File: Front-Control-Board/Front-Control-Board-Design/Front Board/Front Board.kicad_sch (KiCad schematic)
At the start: 16 parts, among them J1 Conn_01x08, J2 Conn_01x23, U1 MAX33054EASA+T, U2 NCP1117-5.0_TO252, U3 ESP32-WROOM-32D

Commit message: front board update
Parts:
- added D? (x3): 1N630xCA, Diode_THT:D_DO-201AE_P15.24mm_Horizontal, symbol Diode:1N630xCA
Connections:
- net Brake_1: now also D?.2 (K)
- net CAN_RX: now also U3.17 (SHD/SD2)
- net CAN_TX: now also U3.18 (SWP/SD3)
- net D+: now also D?.1 (A1)
- net D-: now also D?.1 (A1)
- net GND: now also D?.1 (A1), D?.2 (A2), D?.2 (A2)
- net L_wheel: now also D?.1 (K)
- net R_sus: now also D?.2 (K)
- net R_wheel: now also D?.1 (K)
- net VBUS: now also D?.2 (A2)
- net LORA_RX: now reaches U3.27 (IO16)
- net LORA_TX: now reaches U3.28 (IO17)
- net LORA NSS: now reaches U3.30 (IO18)
- net LORA Reset: now reaches U3.31 (IO19)
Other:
- removed sheet USB interface
- added sheet USB-interface (USB-interface.kicad_sch)
- moved on the sheet: D?

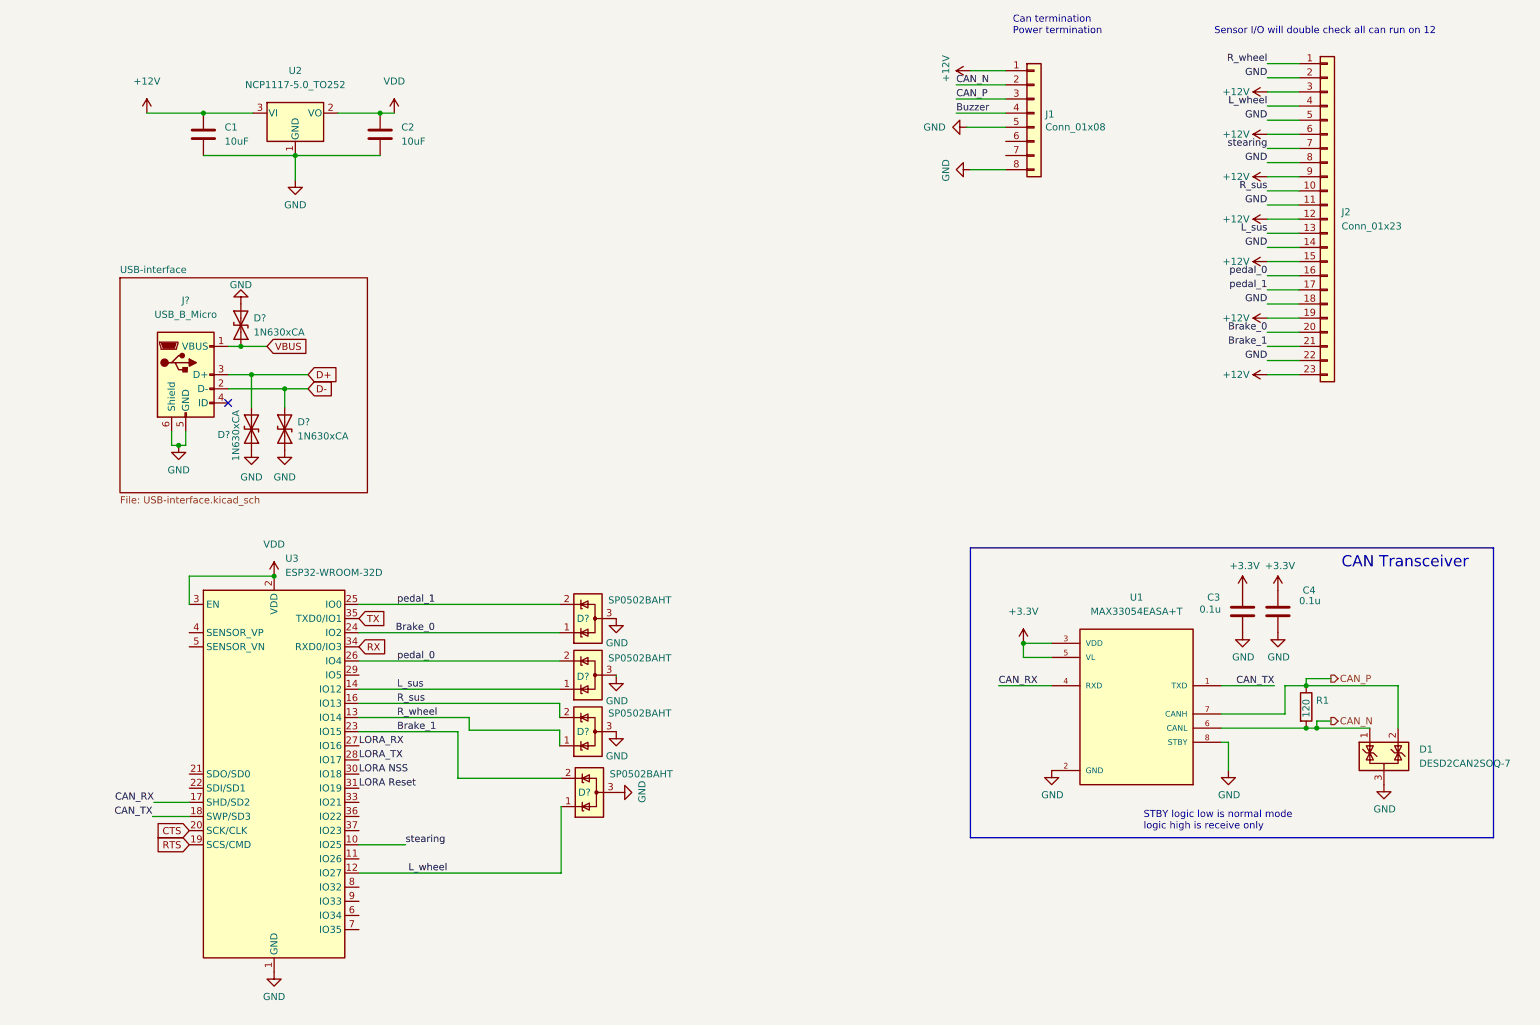
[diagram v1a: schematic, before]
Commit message: Front board finished schematic
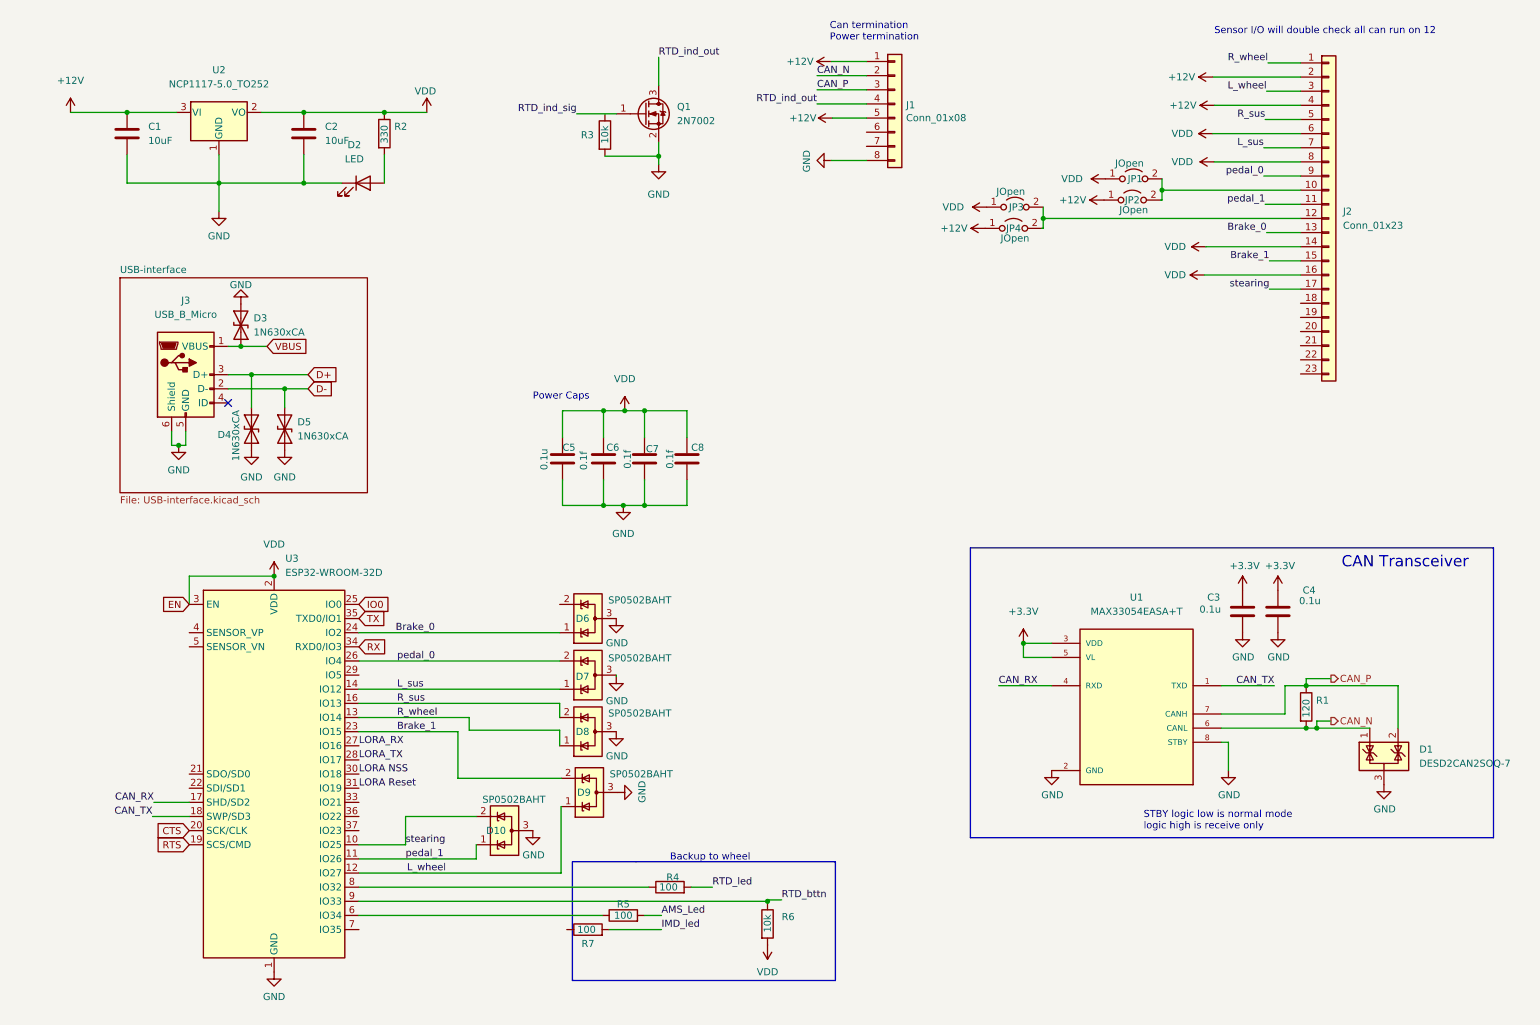
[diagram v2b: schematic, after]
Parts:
- added C5: 0.1u, Capacitor_SMD:C_0603_1608Metric_Pad1.08x0.95mm_HandSolder, symbol Device:C
- added C6, C7, C8: 0.1f, Capacitor_SMD:C_0603_1608Metric_Pad1.08x0.95mm_HandSolder, symbol Device:C
- added D10: SP0502BAHT, Package_TO_SOT_SMD:SOT-23, symbol Power_Protection:SP0502BAHT
- added D2: LED, LED_SMD:LED_0603_1608Metric_Pad1.05x0.95mm_HandSolder, symbol Device:LED
- added JP1, JP2, JP3, JP4: JOpen, TestPoint:TestPoint_2Pads_Pitch2.54mm_Drill0.8mm, symbol Jumper:Jumper_2_Open
- added Q1: 2N7002, Package_TO_SOT_SMD:SOT-23, symbol Transistor_FET:2N7002
- added R2: 330, Resistor_SMD:R_0603_1608Metric_Pad0.98x0.95mm_HandSolder, symbol Device:R
- added R3, R6: 10k, Resistor_SMD:R_0603_1608Metric_Pad0.98x0.95mm_HandSolder, symbol Device:R
- added R4, R5, R7: 100, Resistor_SMD:R_0603_1608Metric_Pad0.98x0.95mm_HandSolder, symbol Device:R
- J3: renamed from J?; footprint (none) -> Connector_USB:USB_Micro-B_Wuerth_614105150721_Vertical
- gave numbers to parts that had none: 7
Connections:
- net +12V: now also J1.5 (Pin_5), J2.2 (Pin_2), J2.4 (Pin_4), JP2.1 (A), JP4.1 (A); no longer J2.12 (Pin_12), J2.15 (Pin_15), J2.19 (Pin_19), J2.23 (Pin_23), J2.3 (Pin_3), J2.6 (Pin_6), J2.9 (Pin_9)
- net Brake_0: now also J2.13 (Pin_13); no longer J2.20 (Pin_20)
- net Brake_1: now also J2.15 (Pin_15); no longer J2.21 (Pin_21)
- net GND: now also C5.2, C6.2, C7.2, C8.2, D10.3 (A), D2.1 (K), Q1.2 (S), R3.2; no longer J1.5 (Pin_5), J2.11 (Pin_11), J2.14 (Pin_14), J2.18 (Pin_18), J2.2 (Pin_2), J2.22 (Pin_22), J2.5 (Pin_5), J2.8 (Pin_8)
- net L_sus: now also J2.7 (Pin_7); no longer J2.13 (Pin_13)
- net L_wheel: now also J2.3 (Pin_3); no longer J2.4 (Pin_4)
- net R_sus: now also J2.5 (Pin_5); no longer J2.10 (Pin_10)
- net VDD: now also J2.14 (Pin_14), J2.16 (Pin_16), J2.6 (Pin_6), J2.8 (Pin_8), C5.1, C6.1, C7.1, C8.1, JP1.1 (A), JP3.1 (A), R2.1, R6.2
- net pedal_0: now also J2.9 (Pin_9); no longer J2.16 (Pin_16)
- net pedal_1: now also J2.11 (Pin_11), U3.11 (IO26), D10.1 (K); no longer D6.2 (K), J2.17 (Pin_17), U3.25 (IO0)
- net stearing: now also J2.17 (Pin_17), D10.2 (K); no longer J2.7 (Pin_7)
- net at U3.6 (IO34): now also R5.1
- net at U3.8 (IO32): now also R4.1
- net RTD_bttn: now reaches U3.9 (IO33)
- net RTD_bttn: now also R6.1
- net Buzzer renamed RTD_ind_out
- net RTD_ind_out: now also Q1.3 (D)
- new net: J2.10 (Pin_10), JP1.2 (B), JP2.2 (B)
- new net: J2.12 (Pin_12), JP3.2 (B), JP4.2 (B)
- new net: D2.2 (A), R2.2
- new net AMS_Led: R5.2
- new net IMD_led: R7.2
- new net IO0: U3.25 (IO0)
- new net RTD_ind_sig: Q1.1 (G)
- new net RTD_led: R4.2
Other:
- note added: "Backup to wheel"
- note added: "Power Caps"
- moved on the sheet: C1, C2, J1, U2

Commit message: Front board schematic
and linking to footprint done
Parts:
- J2: footprint (none) -> AERO_Footprints:TE_1-770669-1_23pin_Horizontal
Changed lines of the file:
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@@
       (effects (font (size 1.27 1.27)) (justify left))
     )
-    (property "Footprint" "" (id 2) (at 249.174 52.578 0)
+    (property "Footprint" "AERO_Footprints:TE_1-770669-1_23pin_Horizontal" (id 2) (at 249.174 52.578 0)
       (effects (font (size 1.27 1.27)) hide)
     )
@@
     )
     (path "/197899a5-be91-4fa9-8e75-522cf68d1072"
-      (reference "J2") (unit 1) (value "Conn_01x23") (footprint "")
+      (reference "J2") (unit 1) (value "Conn_01x23") (footprint "AERO_Footprints:TE_1-770669-1_23pin_Horizontal")
     )
     (path "/5026d5ac-936b-4ec5-ab91-2c1c820a0f48"

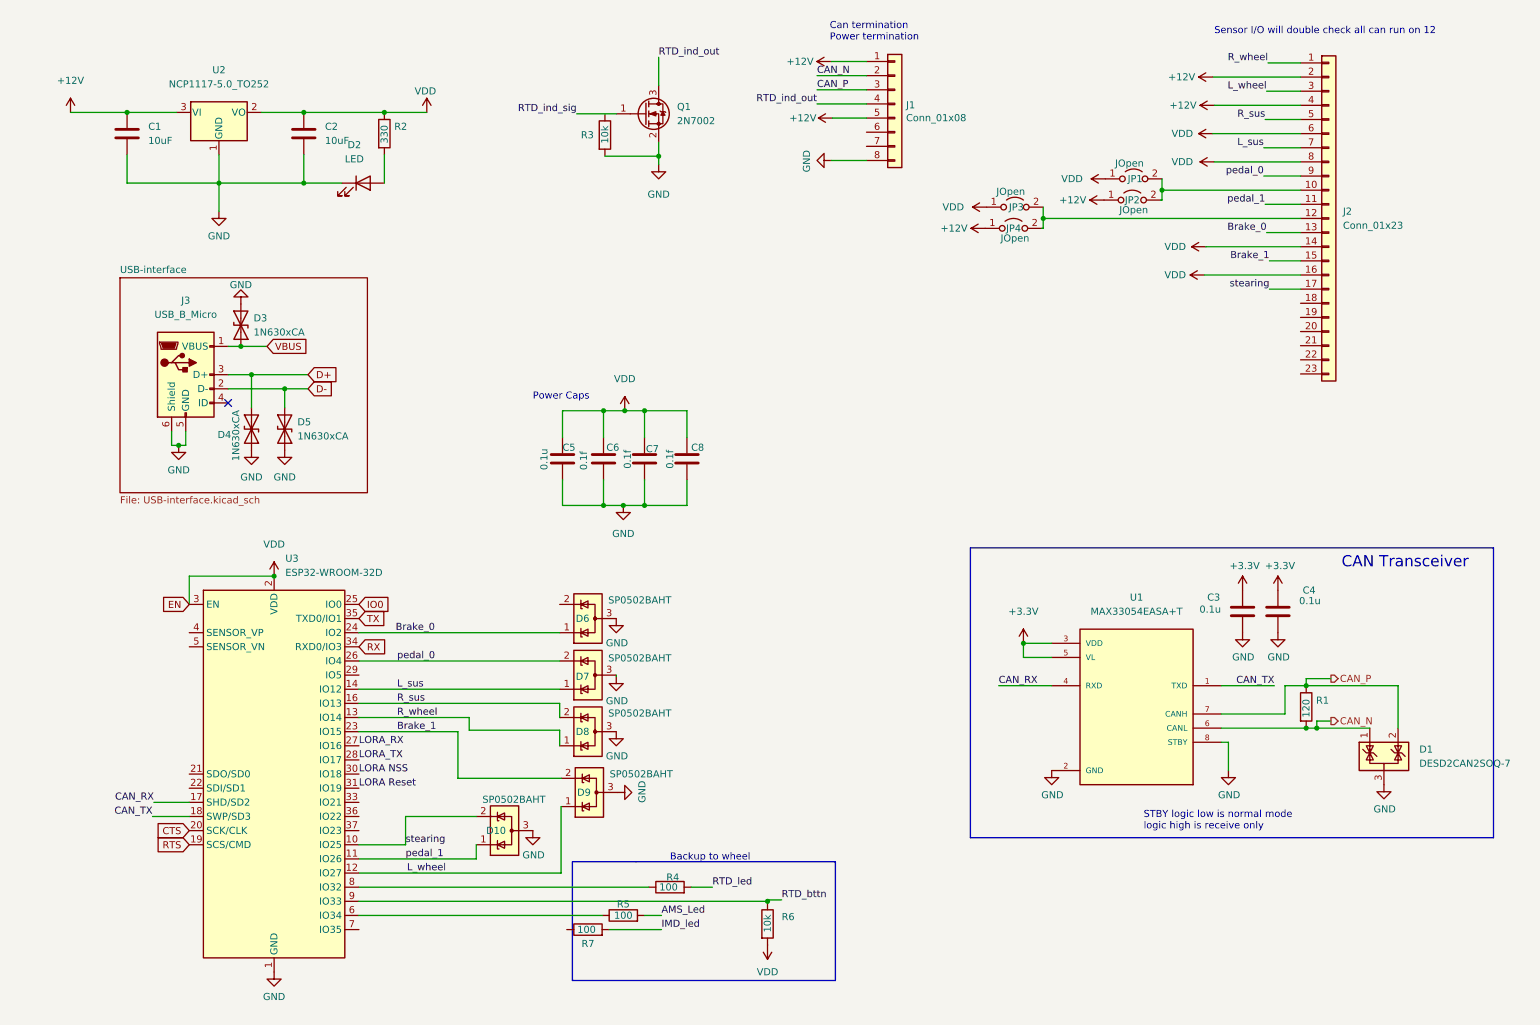
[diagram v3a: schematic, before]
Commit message: front board with footprint
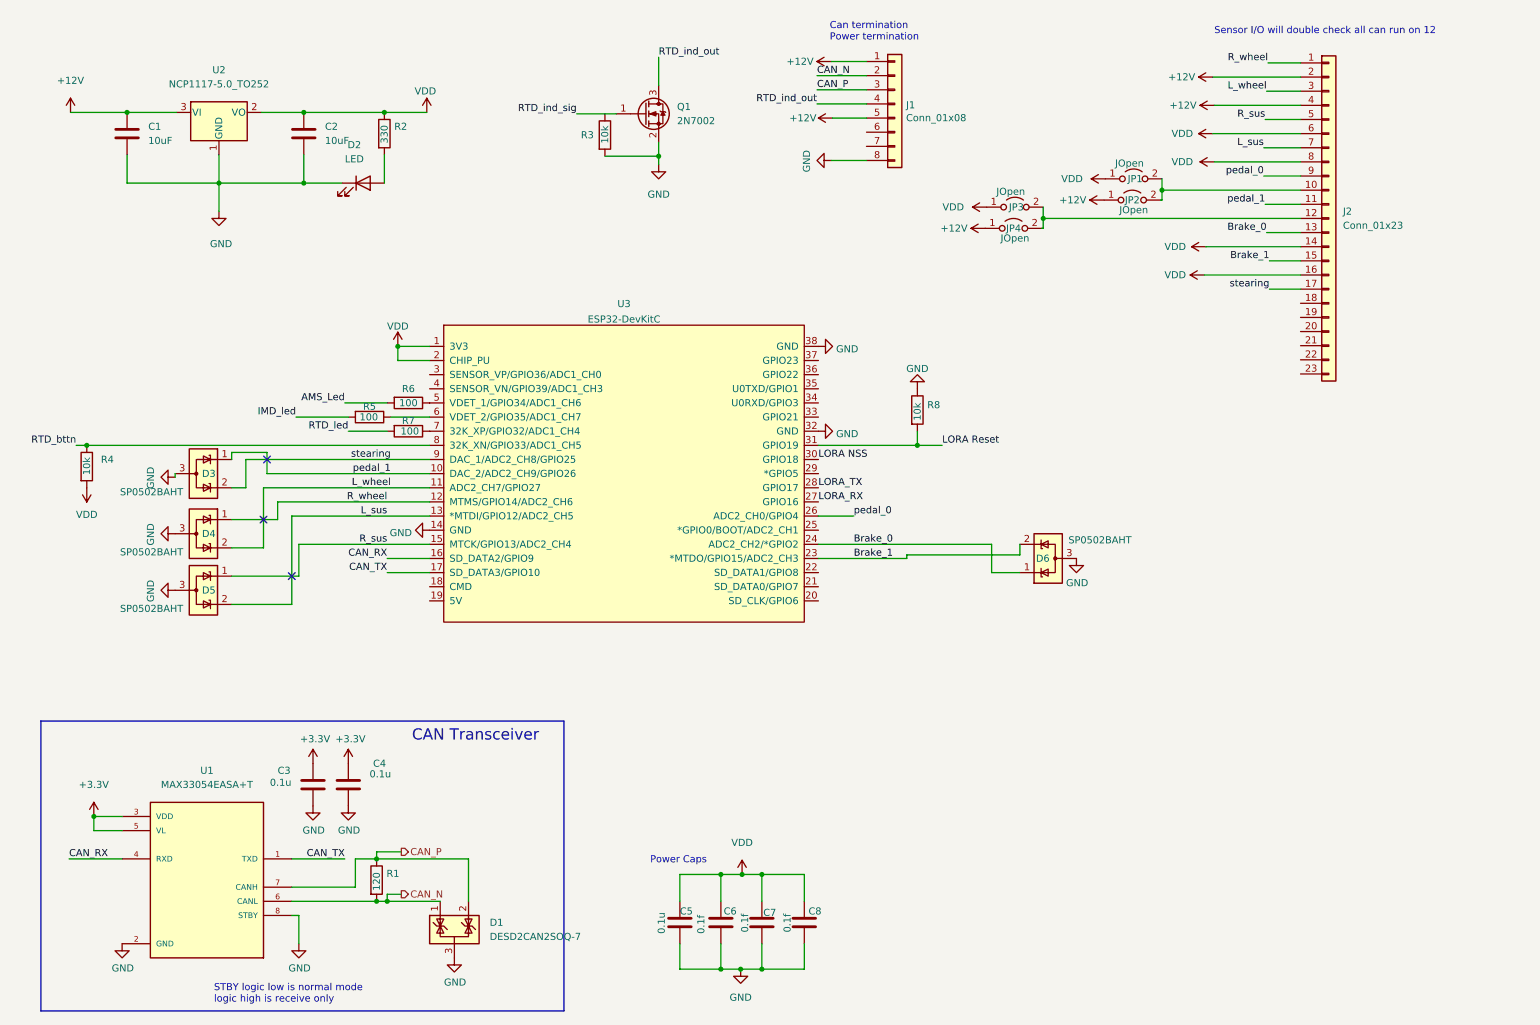
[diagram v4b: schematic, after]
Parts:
- removed D10, D7, D8, D9: SP0502BAHT, Package_TO_SOT_SMD:SOT-23, symbol Power_Protection:SP0502BAHT
- removed D3, D4, D5: 1N630xCA, Diode_THT:D_DO-201AE_P15.24mm_Horizontal, symbol Diode:1N630xCA
- removed J3: USB_B_Micro, Connector_USB:USB_Micro-B_Wuerth_614105150721_Vertical, symbol Connector:USB_B_Micro
- removed U3: ESP32-WROOM-32D, RF_Module:ESP32-WROOM-32, symbol RF_Module:ESP32-WROOM-32D
- added D3, D4, D5: SP0502BAHT, Package_TO_SOT_SMD:SOT-23, symbol Power_Protection:SP0502BAHT
- added R8: 10k, Resistor_SMD:R_0603_1608Metric_Pad0.98x0.95mm_HandSolder, symbol Device:R
- added U3: ESP32-DevKitC, Espressif:ESP32-DevKitC, symbol ESP_32:ESP32-DevKitC
- R4: value 100 -> 10k
- R6: value 10k -> 100
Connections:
- net AMS_Led: now also R6.2; no longer R5.2
- net Brake_0: now also U3.24 (ADC2_CH2/*GPIO2)
- net Brake_1: now also D6.2 (K), U3.23 (*MTDO/GPIO15/ADC2_CH3)
- net CAN_RX: now also U3.16 (SD_DATA2/GPIO9)
- net CAN_TX: now also U3.17 (SD_DATA3/GPIO10)
- net GND: now also D3.3 (A), D4.3 (A), D5.3 (A), R8.1, U3.14 (GND), U3.32 (GND), U3.38 (GND)
- net IMD_led: now also R5.2; no longer R7.2
- net LORA NSS: now also U3.30 (GPIO18)
- net LORA Reset: now also R8.2, U3.31 (GPIO19)
- net LORA_RX: now also U3.27 (GPIO16)
- net LORA_TX: now also U3.28 (GPIO17)
- net L_sus: now also D5.2 (K), U3.13 (*MTDI/GPIO12/ADC2_CH5)
- net L_wheel: now also D4.2 (K), U3.11 (ADC2_CH7/GPIO27)
- net RTD_bttn: now also R4.1, U3.8 (32K_XN/GPIO33/ADC1_CH5); no longer R6.1
- net RTD_led: now also R7.2; no longer R4.2
- net R_sus: now also D5.1 (K), U3.15 (MTCK/GPIO13/ADC2_CH4)
- net R_wheel: now also D4.1 (K), U3.12 (MTMS/GPIO14/ADC2_CH6)
- net VDD: now also R4.2, U3.1 (3V3), U3.2 (CHIP_PU); no longer R6.2
- net pedal_0: now also U3.26 (ADC2_CH0/GPIO4)
- net pedal_1: now also D3.1 (K), U3.10 (DAC_2/ADC2_CH9/GPIO26)
- net stearing: now also D3.2 (K), U3.9 (DAC_1/ADC2_CH8/GPIO25)
- net at R5.1: now also U3.6 (VDET_2/GPIO35/ADC1_CH7)
- net at R7.1: now also U3.7 (32K_XP/GPIO32/ADC1_CH4)
- new net: R6.1, U3.5 (VDET_1/GPIO34/ADC1_CH6)
- no-connect marks 1 -> 3
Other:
- removed sheet USB-interface
- note removed: "Backup to wheel"
- moved on the sheet: C3, C4, C5, C6, C7, C8, D1, R1, U1

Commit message: Update
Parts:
- removed C7, C8: 0.1f, Capacitor_SMD:C_0603_1608Metric_Pad1.08x0.95mm_HandSolder, symbol Device:C
- removed JP1, JP2, JP3, JP4: JOpen, TestPoint:TestPoint_2Pads_Pitch2.54mm_Drill0.8mm, symbol Jumper:Jumper_2_Open
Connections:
- net +12V: now also J1.7 (Pin_7), J2.16 (Pin_16); no longer J1.1 (Pin_1), J1.5 (Pin_5), J2.2 (Pin_2), J2.4 (Pin_4)
- net AMS_Led: now also J2.22 (Pin_22)
- net CAN_N: now also J1.4 (Pin_4); no longer J1.2 (Pin_2)
- net CAN_P: now also J1.5 (Pin_5); no longer J1.3 (Pin_3)
- net IMD_led: now also J2.23 (Pin_23)
- net LORA NSS: now also J2.19 (Pin_19)
- net LORA Reset: now also J2.18 (Pin_18)
- net LORA_RX: now also J2.20 (Pin_20)
- net LORA_TX: now also J2.21 (Pin_21)
- net RTD_ind_out: now also J1.6 (Pin_6); no longer J1.4 (Pin_4)
- net VDD: now also J2.10 (Pin_10), J2.12 (Pin_12), J2.2 (Pin_2), J2.4 (Pin_4); no longer J2.16 (Pin_16)

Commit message: Colin Push
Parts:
- removed C5: 0.1u, Capacitor_SMD:C_0603_1608Metric_Pad1.08x0.95mm_HandSolder, symbol Device:C
- removed C6: 0.1f, Capacitor_SMD:C_0603_1608Metric_Pad1.08x0.95mm_HandSolder, symbol Device:C
- added D7: TS4148C RZG, Diode_SMD:D_0603_1608Metric_Pad1.05x0.95mm_HandSolder, symbol Device:D
- U2: value NCP1117-5.0_TO252 -> TS2940CP33 ROG
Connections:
- net +12V: now also J2.18 (Pin_18), D7.1 (K); no longer J1.7 (Pin_7)
- net Brake_0: now also J1.7 (Pin_7); no longer J2.13 (Pin_13)
- net Brake_1: now also J1.8 (Pin_8); no longer J2.15 (Pin_15)
- net CAN_N: now also J2.20 (Pin_20); no longer J1.4 (Pin_4)
- net CAN_P: now also J2.21 (Pin_21); no longer J1.5 (Pin_5)
- net GND: now also J1.1 (Pin_1), D7.2 (A); no longer J1.8 (Pin_8)
- net LORA NSS: now also J1.2 (Pin_2); no longer J2.19 (Pin_19)
- net LORA Reset: now also J1.3 (Pin_3); no longer J2.18 (Pin_18)
- net LORA_RX: now also J1.4 (Pin_4); no longer J2.20 (Pin_20)
- net LORA_TX: now also J1.5 (Pin_5); no longer J2.21 (Pin_21)
- net RTD_ind_out: now also J2.15 (Pin_15), J2.19 (Pin_19); no longer J1.6 (Pin_6)
- net RTD_ind_sig: now also R3.1, U3.3 (SENSOR_VP/GPIO36/ADC1_CH0)
- net pedal_0: now also J1.6 (Pin_6); no longer J2.9 (Pin_9)
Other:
- note removed: "Can termination Power termination"
- note removed: "Power Caps"

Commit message: Front board first draft
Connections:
- net +3V3 is gone; now on net VDD: C3.1, C4.1, U1.3 (VDD), U1.5 (VL)
- net +12V: now also J2.22 (Pin_22), J2.23 (Pin_23); no longer J2.16 (Pin_16), J2.18 (Pin_18)
- net AMS_Led: now also J2.9 (Pin_9); no longer J2.22 (Pin_22)
- net CAN_N: now also J2.8 (Pin_8); no longer J2.20 (Pin_20)
- net CAN_P: now also J2.15 (Pin_15); no longer J2.21 (Pin_21)
- net IMD_led: now also J2.2 (Pin_2); no longer J2.23 (Pin_23)
- net L_sus: now also J2.13 (Pin_13); no longer J2.7 (Pin_7)
- net L_wheel: now also J2.12 (Pin_12); no longer J2.3 (Pin_3)
- net RTD_bttn: now also J2.3 (Pin_3)
- net RTD_ind_out: now also J2.1 (Pin_1); no longer J2.15 (Pin_15), J2.19 (Pin_19)
- net RTD_led: now also J2.10 (Pin_10)
- net R_sus: now also J2.6 (Pin_6); no longer J2.5 (Pin_5)
- net R_wheel: now also J2.5 (Pin_5); no longer J2.1 (Pin_1)
- net VDD: now also J2.16 (Pin_16), J2.17 (Pin_17), J2.18 (Pin_18), J2.19 (Pin_19), J2.20 (Pin_20), J2.21 (Pin_21); no longer J2.10 (Pin_10), J2.12 (Pin_12), J2.2 (Pin_2), J2.4 (Pin_4), J2.6 (Pin_6), J2.8 (Pin_8)
- net pedal_1: now also J2.4 (Pin_4); no longer J2.11 (Pin_11)
- net stearing: now also J2.11 (Pin_11); no longer J2.17 (Pin_17)
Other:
- note removed: "Sensor I/O will double check all can run on 12"
